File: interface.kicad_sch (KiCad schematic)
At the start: 4 parts

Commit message: Assign footprints
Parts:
- USB_Default_Power_CC1, USB_Default_Power_CC2: footprint (none) -> Resistor_SMD:R_0603_1608Metric
- Wired_Interface0: footprint USB4105-GF-A:GCT_USB4105-GF-A -> GCT_USB4105-GF-A
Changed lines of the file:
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@@
 			)
 		)
-		(property "Footprint" ""
+		(property "Footprint" "Resistor_SMD:R_0603_1608Metric"
 			(at 105.156 42.926 90)
 			(effects
@@
 			)
 		)
-		(property "Datasheet" "~"
+		(property "Datasheet" "https://www.digikey.com/en/products/detail/stackpole-electronics-inc/RMCF0603FT5K10/1760908"
 			(at 105.41 41.91 0)
 			(effects
@@
 			)
 		)
-		(property "Footprint" "USB4105-GF-A:GCT_USB4105-GF-A"
+		(property "Footprint" "GCT_USB4105-GF-A"
 			(at 144.78 46.99 0)
 			(effects
@@
 			)
 		)
-		(property "Footprint" ""
+		(property "Footprint" "Resistor_SMD:R_0603_1608Metric"
 			(at 183.134 42.926 90)
 			(effects
@@
 			)
 		)
-		(property "Datasheet" "~"
+		(property "Datasheet" "https://www.digikey.com/en/products/detail/stackpole-electronics-inc/RMCF0603FT5K10/1760908"
 			(at 182.88 41.91 0)
 			(effects

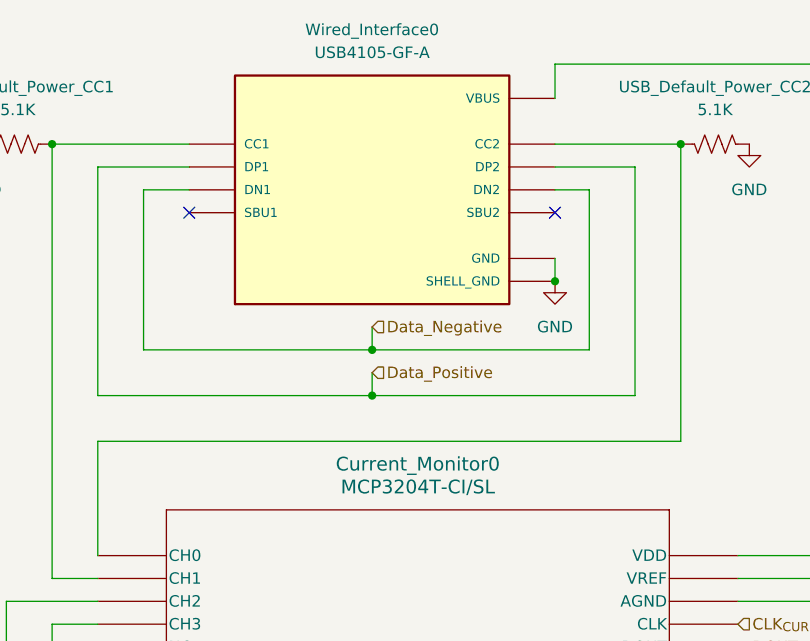
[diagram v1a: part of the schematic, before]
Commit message: Init right and left PCBs
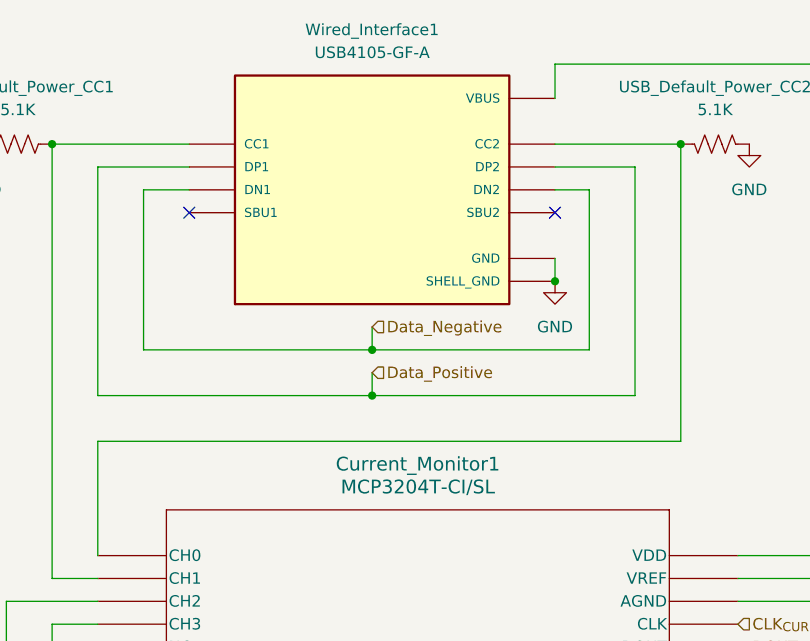
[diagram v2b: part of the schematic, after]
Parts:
- renumbered Current_Monitor0 to Current_Monitor1, Wired_Interface0 to Wired_Interface1
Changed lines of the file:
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@@
+				)
+			)
+			(project "right_hand"
+				(path "/efcccfe8-5e20-4b1b-8d3b-61fce771481e/cd3314d0-f605-42f0-be2b-644cabc7637c"
+					(reference "USB_Default_Power_CC1")
+					(unit 1)
 				)
 			)
@@
 		(dnp no)
 		(fields_autoplaced yes)
-		(property "Reference" "#PWR04"
+		(property "Reference" "#PWR0105"
 			(at 114.3 109.22 0)
 			(effects
@@
 				(path "/06a6eca0-edda-4cc0-a23f-017602e67f07/99f3b279-b2b0-4dd5-ab05-9b518546ce95/cd3314d0-f605-42f0-be2b-644cabc7637c"
 					(reference "#PWR04")
+					(unit 1)
+				)
+			)
+			(project "right_hand"
+				(path "/efcccfe8-5e20-4b1b-8d3b-61fce771481e/cd3314d0-f605-42f0-be2b-644cabc7637c"
+					(reference "#PWR0105")
 					(unit 1)
 				)
@@
 		(dnp no)
 		(fields_autoplaced yes)
-		(property "Reference" "#PWR01"
+		(property "Reference" "#PWR0103"
 			(at 165.1 63.5 0)
 			(effects
@@
 				(path "/06a6eca0-edda-4cc0-a23f-017602e67f07/99f3b279-b2b0-4dd5-ab05-9b518546ce95/cd3314d0-f605-42f0-be2b-644cabc7637c"
 					(reference "#PWR01")
+					(unit 1)
+				)
+			)
+			(project "right_hand"
+				(path "/efcccfe8-5e20-4b1b-8d3b-61fce771481e/cd3314d0-f605-42f0-be2b-644cabc7637c"
+					(reference "#PWR0103")
 					(unit 1)
 				)
@@
 		(dnp no)
 		(fields_autoplaced yes)
-		(property "Reference" "Current_Monitor0"
+		(property "Reference" "Current_Monitor1"
 			(at 149.86 77.47 0)
 			(effects
@@
 				(path "/06a6eca0-edda-4cc0-a23f-017602e67f07/99f3b279-b2b0-4dd5-ab05-9b518546ce95/cd3314d0-f605-42f0-be2b-644cabc7637c"
 					(reference "Current_Monitor0")
+					(unit 1)
+				)
+			)
+			(project "right_hand"
+				(path "/efcccfe8-5e20-4b1b-8d3b-61fce771481e/cd3314d0-f605-42f0-be2b-644cabc7637c"
+					(reference "Current_Monitor1")
 					(unit 1)
 				)
@@
 		(dnp no)
 		(fields_autoplaced yes)
-		(property "Reference" "#PWR03"
+		(property "Reference" "#PWR0101"
 			(at 186.69 48.26 0)
 			(effects
@@
 				(path "/06a6eca0-edda-4cc0-a23f-017602e67f07/99f3b279-b2b0-4dd5-ab05-9b518546ce95/cd3314d0-f605-42f0-be2b-644cabc7637c"
 					(reference "#PWR03")
+					(unit 1)
+				)
+			)
+			(project "right_hand"
+				(path "/efcccfe8-5e20-4b1b-8d3b-61fce771481e/cd3314d0-f605-42f0-be2b-644cabc7637c"
+					(reference "#PWR0101")
 					(unit 1)
 				)
@@
 		(dnp no)
 		(fields_autoplaced yes)
-		(property "Reference" "#PWR05"
+		(property "Reference" "#PWR0102"
 			(at 205.74 99.06 0)
 			(effects
@@
 				(path "/06a6eca0-edda-4cc0-a23f-017602e67f07/99f3b279-b2b0-4dd5-ab05-9b518546ce95/cd3314d0-f605-42f0-be2b-644cabc7637c"
 					(reference "#PWR05")
+					(unit 1)
+				)
+			)
+			(project "right_hand"
+				(path "/efcccfe8-5e20-4b1b-8d3b-61fce771481e/cd3314d0-f605-42f0-be2b-644cabc7637c"
+					(reference "#PWR0102")
 					(unit 1)
 				)
@@
 		(dnp no)
 		(fields_autoplaced yes)
-		(property "Reference" "#PWR02"
+		(property "Reference" "#PWR0104"
 			(at 101.6 48.26 0)
 			(effects
@@
 				(path "/06a6eca0-edda-4cc0-a23f-017602e67f07/99f3b279-b2b0-4dd5-ab05-9b518546ce95/cd3314d0-f605-42f0-be2b-644cabc7637c"
 					(reference "#PWR02")
+					(unit 1)
+				)
+			)
+			(project "right_hand"
+				(path "/efcccfe8-5e20-4b1b-8d3b-61fce771481e/cd3314d0-f605-42f0-be2b-644cabc7637c"
+					(reference "#PWR0104")
 					(unit 1)
 				)
@@
 		(dnp no)
 		(fields_autoplaced yes)
-		(property "Reference" "Wired_Interface0"
+		(property "Reference" "Wired_Interface1"
 			(at 144.78 29.21 0)
 			(effects
@@
 				(path "/06a6eca0-edda-4cc0-a23f-017602e67f07/99f3b279-b2b0-4dd5-ab05-9b518546ce95/cd3314d0-f605-42f0-be2b-644cabc7637c"
 					(reference "Wired_Interface0")
+					(unit 1)
+				)
+			)
+			(project "right_hand"
+				(path "/efcccfe8-5e20-4b1b-8d3b-61fce771481e/cd3314d0-f605-42f0-be2b-644cabc7637c"
+					(reference "Wired_Interface1")
 					(unit 1)
 				)
@@
 				)
 			)
+			(project "right_hand"
+				(path "/efcccfe8-5e20-4b1b-8d3b-61fce771481e/cd3314d0-f605-42f0-be2b-644cabc7637c"
+					(reference "USB_Default_Power_CC2")
+					(unit 1)
+				)
+			)
 		)
 	)
@@
 				)
 			)
+			(project "right_hand"
+				(path "/efcccfe8-5e20-4b1b-8d3b-61fce771481e/cd3314d0-f605-42f0-be2b-644cabc7637c"
+					(page "3")
+				)
+			)

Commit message: Rename keyswitch diodes
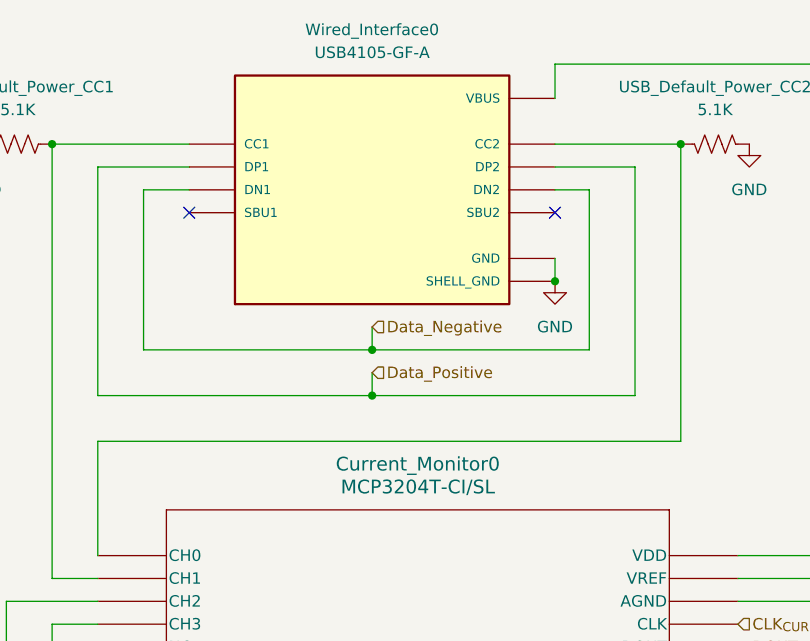
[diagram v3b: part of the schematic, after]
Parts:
- renumbered Current_Monitor1 to Current_Monitor0, Wired_Interface1 to Wired_Interface0
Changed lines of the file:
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@@
 		(dnp no)
 		(fields_autoplaced yes)
-		(property "Reference" "#PWR0105"
+		(property "Reference" "#PWR04"
 			(at 114.3 109.22 0)
 			(effects
@@
 		(dnp no)
 		(fields_autoplaced yes)
-		(property "Reference" "#PWR0103"
+		(property "Reference" "#PWR01"
 			(at 165.1 63.5 0)
 			(effects
@@
 		(dnp no)
 		(fields_autoplaced yes)
-		(property "Reference" "Current_Monitor1"
+		(property "Reference" "Current_Monitor0"
 			(at 149.86 77.47 0)
 			(effects
@@
 		(dnp no)
 		(fields_autoplaced yes)
-		(property "Reference" "#PWR0101"
+		(property "Reference" "#PWR03"
 			(at 186.69 48.26 0)
 			(effects
@@
 		(dnp no)
 		(fields_autoplaced yes)
-		(property "Reference" "#PWR0102"
+		(property "Reference" "#PWR05"
 			(at 205.74 99.06 0)
 			(effects
@@
 		(dnp no)
 		(fields_autoplaced yes)
-		(property "Reference" "#PWR0104"
+		(property "Reference" "#PWR02"
 			(at 101.6 48.26 0)
 			(effects
@@
 		(dnp no)
 		(fields_autoplaced yes)
-		(property "Reference" "Wired_Interface1"
+		(property "Reference" "Wired_Interface0"
 			(at 144.78 29.21 0)
 			(effects

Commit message: Size up components
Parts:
- USB_Default_Power_CC1, USB_Default_Power_CC2: footprint Resistor_SMD:R_0603_1608Metric -> Resistor_SMD:R_0805_2012Metric
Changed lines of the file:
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@@
 			)
 		)
-		(property "Footprint" "Resistor_SMD:R_0603_1608Metric"
+		(property "Footprint" "Resistor_SMD:R_0805_2012Metric"
 			(at 105.156 42.926 90)
 			(effects
@@
 			)
 		)
-		(property "Datasheet" "https://www.digikey.com/en/products/detail/stackpole-electronics-inc/RMCF0603FT5K10/1760908"
+		(property "Datasheet" "https://www.digikey.com/en/products/detail/stackpole-electronics-inc/RNCF0805DTE5K10/6241868"
 			(at 105.41 41.91 0)
 			(effects
@@
 			)
 		)
-		(property "Footprint" "Resistor_SMD:R_0603_1608Metric"
+		(property "Footprint" "Resistor_SMD:R_0805_2012Metric"
 			(at 183.134 42.926 90)
 			(effects
@@
 			)
 		)
-		(property "Datasheet" "https://www.digikey.com/en/products/detail/stackpole-electronics-inc/RMCF0603FT5K10/1760908"
+		(property "Datasheet" "https://www.digikey.com/en/products/detail/stackpole-electronics-inc/RNCF0805DTE5K10/6241868"
 			(at 182.88 41.91 0)
 			(effects
